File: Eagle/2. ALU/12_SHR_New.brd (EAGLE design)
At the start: 160 x 100 mm, 7 parts, among them IC3 74LS126N, IC4 74LS126N

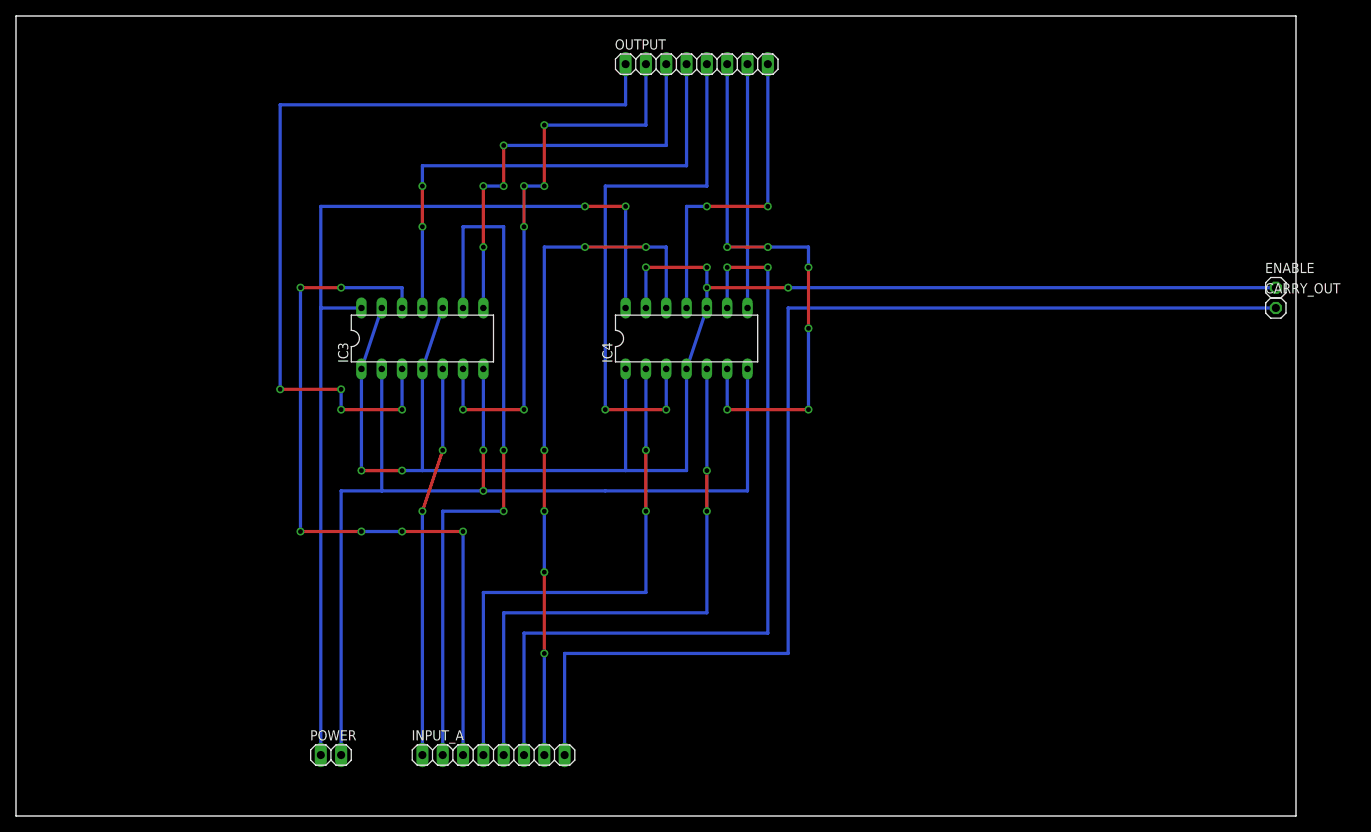
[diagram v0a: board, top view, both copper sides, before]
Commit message: Added new schematics.
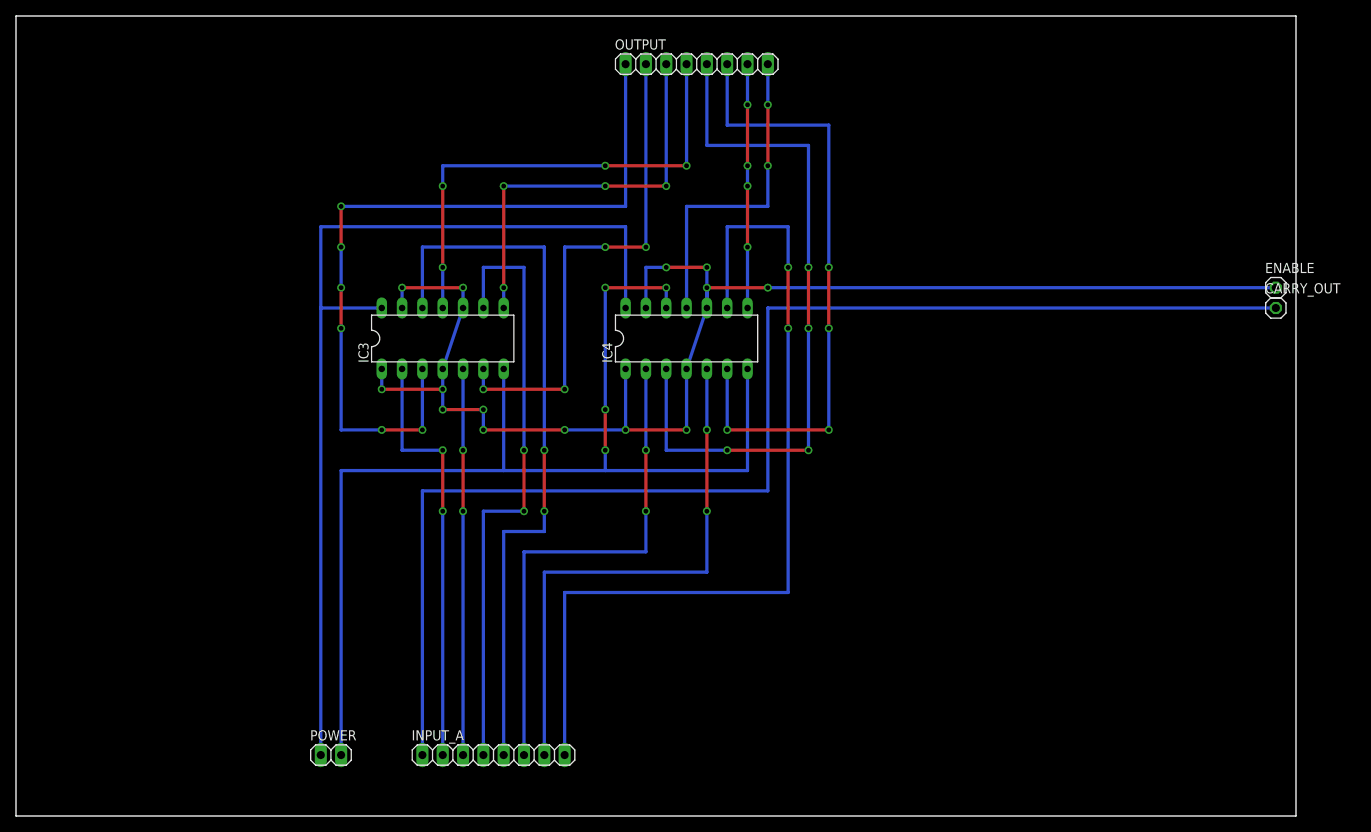
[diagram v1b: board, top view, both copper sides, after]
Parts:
- moved IC3 2.54 mm to (53.3, 59.7)
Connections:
- removed net N$1: IC3.5, INPUT_A.1
- removed net N$13: IC4.12, INPUT_A.7
- removed net N$9: IC4.5, INPUT_A.5
- new net N$6: IC3.12, INPUT_A.5
- new net N$7: IC4.2, INPUT_A.6
- new net N$8: IC4.5, INPUT_A.7
- net GND: now also IC4.12; no longer IC3.2
- net N$11: now also INPUT_A.8; no longer INPUT_A.6
- net N$2: now also INPUT_A.1; no longer INPUT_A.8
- net N$20: now also IC3.5; no longer IC3.12
- net N$21: now also IC3.9; no longer IC4.2
- net N$3: now also IC3.2; no longer IC3.9
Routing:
- net N$6: track 0.00 -> 91.4 mm, vias 0 -> 2
- net N$13: track 86.4 -> 0.00 mm, vias 6 -> 0
- net N$9: track 73.7 -> 0.00 mm, vias 2 -> 0
- net N$8: track 0.00 -> 68.6 mm, vias 0 -> 2
- net N$7: track 0.00 -> 63.5 mm, vias 0 -> 2
- net N$1: track 48.7 -> 0.00 mm, vias 2 -> 0
- net N$20: track 94.0 -> 48.3 mm, vias 6 -> 2
- net N$3: track 88.9 -> 53.3 mm
- net N$33: track 204.4 -> 183.7 mm, vias 6 -> 14
- net N$29: track 68.6 -> 88.9 mm, vias 2 -> 4
- net N$2: track 144.8 -> 162.6 mm
- net GND: track 129.5 -> 144.8 mm, vias 2 -> 4
- net N$11: track 101.6 -> 111.8 mm
- net N$30: track 68.6 -> 78.7 mm, vias 6 -> 4
- net N$26: track 71.1 -> 63.5 mm, vias 6 -> 4
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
